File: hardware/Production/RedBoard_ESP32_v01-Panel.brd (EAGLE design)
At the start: 246.1 x 248.9 mm, 2478 parts, among them J1 5.5x2.1mm Barrel, J101 USB C, J102 USB_SOLDER_PADS, J103 M10NO_SILK, J108 QWIIC_RIGHT_ANGLE, J109 MICRO-SD-PUSH-PUSH-EXT-PIN, J110 5.5x2.1mm Barrel, J117 USB C, J118 USB_SOLDER_PADS, J119 M10NO_SILK, J124 QWIIC_RIGHT_ANGLE, J125 MICRO-SD-PUSH-PUSH-EXT-PIN, J126 5.5x2.1mm Barrel, J13 QWIIC_RIGHT_ANGLE, J133 USB C, J134 USB_SOLDER_PADS, J135 M10NO_SILK, J140 QWIIC_RIGHT_ANGLE, J141 MICRO-SD-PUSH-PUSH-EXT-PIN, J142 5.5x2.1mm Barrel, J149 USB C, J15 MICRO-SD-PUSH-PUSH-EXT-PIN, J150 USB_SOLDER_PADS, J151 M10NO_SILK, J156 QWIIC_RIGHT_ANGLE, J157 MICRO-SD-PUSH-PUSH-EXT-PIN, J158 5.5x2.1mm Barrel, J165 USB C, J166 USB_SOLDER_PADS, J167 M10NO_SILK, J172 QWIIC_RIGHT_ANGLE, J173 MICRO-SD-PUSH-PUSH-EXT-PIN, J174 5.5x2.1mm Barrel, J181 USB C, J182 USB_SOLDER_PADS, J183 M10NO_SILK, J188 QWIIC_RIGHT_ANGLE, J189 MICRO-SD-PUSH-PUSH-EXT-PIN, J190 5.5x2.1mm Barrel, J2 USB C, J21 USB C, J22 USB_SOLDER_PADS, J23 M10NO_SILK, J28 QWIIC_RIGHT_ANGLE, J29 MICRO-SD-PUSH-PUSH-EXT-PIN, J3 USB_SOLDER_PADS, J30 5.5x2.1mm Barrel, J37 USB C, J38 USB_SOLDER_PADS, J39 M10NO_SILK, J44 QWIIC_RIGHT_ANGLE, J45 MICRO-SD-PUSH-PUSH-EXT-PIN, J46 5.5x2.1mm Barrel, J5 M10NO_SILK, J53 USB C, J54 USB_SOLDER_PADS, J55 M10NO_SILK, J60 QWIIC_RIGHT_ANGLE, J61 MICRO-SD-PUSH-PUSH-EXT-PIN, J62 5.5x2.1mm Barrel, J69 USB C, J70 USB_SOLDER_PADS, J71 M10NO_SILK, J76 QWIIC_RIGHT_ANGLE, J77 MICRO-SD-PUSH-PUSH-EXT-PIN, J78 5.5x2.1mm Barrel, J85 USB C, J86 USB_SOLDER_PADS, J87 M10NO_SILK, J92 QWIIC_RIGHT_ANGLE, J93 MICRO-SD-PUSH-PUSH-EXT-PIN, J94 5.5x2.1mm Barrel, Q1 MBT3904DW1T1, Q100 20V/4.2A/52mΩ/1.4W, Q102 20V/4.2A/52mΩ/1.4W, Q104 20V/4.2A/52mΩ/1.4W, Q105 MBT3904DW1T1, Q107 20V/4.2A/52mΩ/1.4W, Q109 20V/4.2A/52mΩ/1.4W, Q11 20V/4.2A/52mΩ/1.4W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

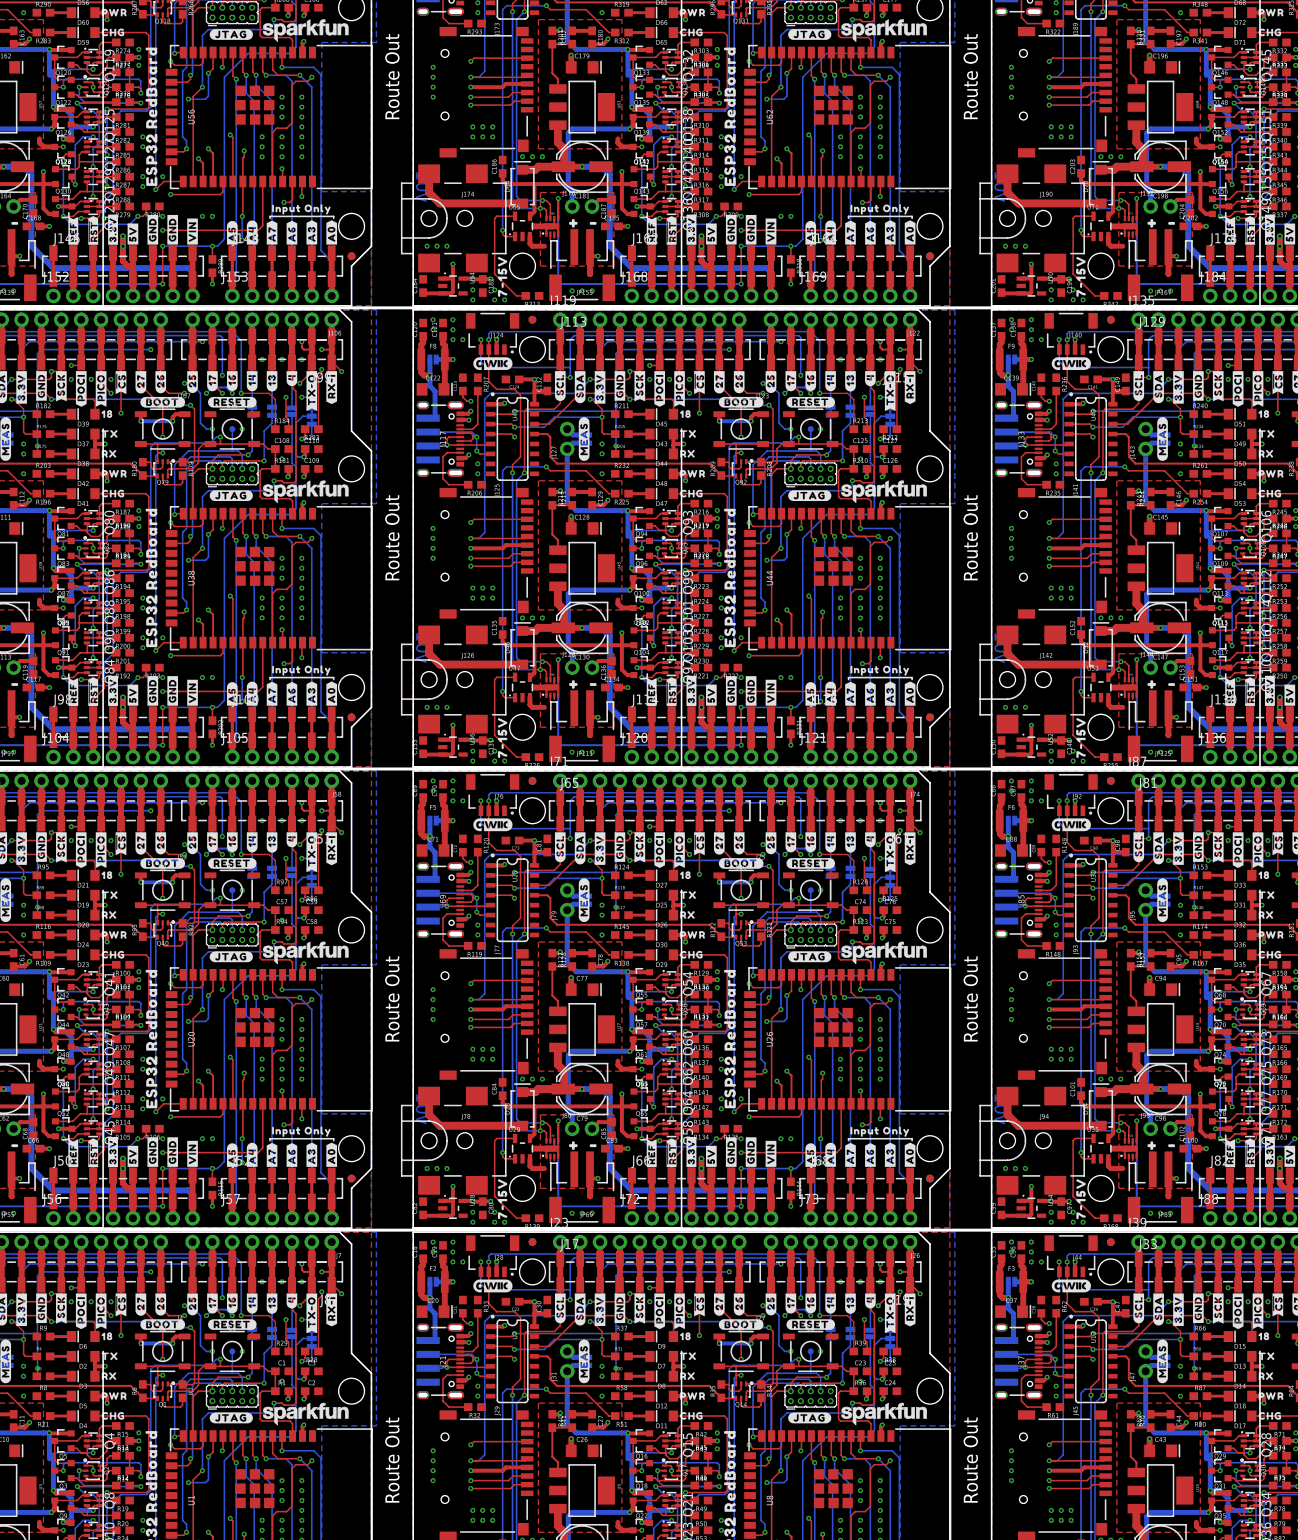
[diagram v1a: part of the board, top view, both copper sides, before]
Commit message: Fixed trace on bottom side, regenerated panel file.
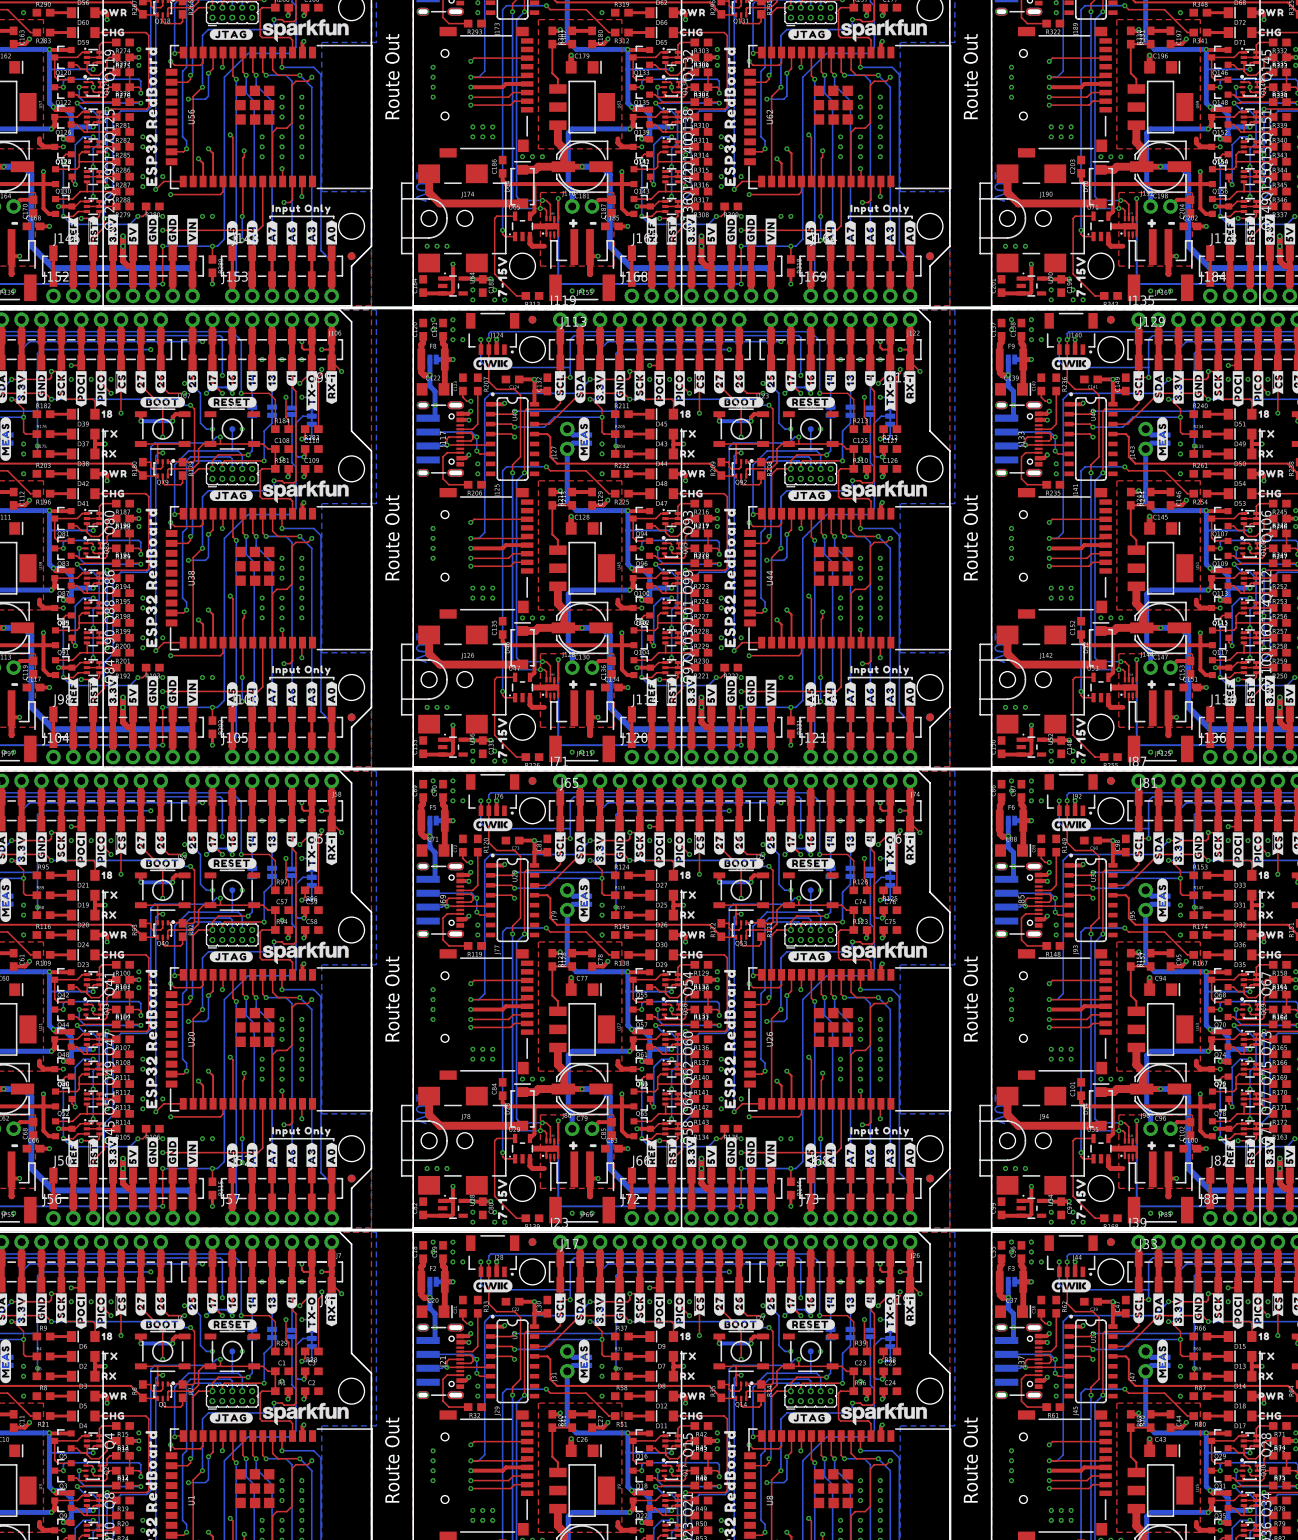
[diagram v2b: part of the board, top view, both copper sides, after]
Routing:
- net 5V_MEAS1: track 65.2 -> 64.6 mm
- net 5V_MEAS8: track 65.2 -> 64.6 mm
- net 5V_MEAS5: track 65.2 -> 64.6 mm
- net 5V_MEAS4: track 65.2 -> 64.6 mm
- net 5V_MEAS10: track 65.2 -> 64.6 mm
- net 5V_MEAS: track 65.2 -> 64.6 mm
- net 5V_MEAS9: track 65.2 -> 64.6 mm
- net 5V_MEAS7: track 65.2 -> 64.6 mm
- net 5V_MEAS6: track 65.2 -> 64.6 mm
- net 5V_MEAS3: track 65.2 -> 64.6 mm
- net 5V_MEAS11: track 65.2 -> 64.6 mm
- net 5V_MEAS2: track 65.2 -> 64.6 mm

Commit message: Changed labels as suggested by Chris; updated production files.
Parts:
- added U$1141: (no value), output-ESP32:#13#TCK#32321869
- added U$1142: (no value), output-ESP32:#14#TMS#32321869
- added U$1143: (no value), output-ESP32:#16#32321869
- added U$1144: (no value), output-ESP32:#17#32321869
- added U$1145: (no value), output-ESP32:#25#32321869
- added U$1146: (no value), output-ESP32:#26#32321869
- added U$1147: (no value), output-ESP32:#5##CS##32321869
- added U$1148: (no value), output-ESP32:#23#PICO#321866
- added U$1149: (no value), output-ESP32:#19#POCI#321866
- added U$1150: (no value), output-ESP32:#18#SCK#32321869
- added U$1151: (no value), output-ESP32:#21#SDA#32321869
- added U$1152: (no value), output-ESP32:#22#SCL#32321869
- added U$1153: (no value), output-ESP32:#27#32321869
- added U$1154: (no value), output-ESP32:#GND#321866
- added U$1155: (no value), output-ESP32:#3#3V#321866
- added U$1156: (no value), output-ESP32:#MEAS#1851
- added U$1157: (no value), output-ESP32:#BYP#35
- added U$1158: (no value), output-ESP32:D#32321863
- added U$1159: (no value), output-ESP32:D#32321862
- added U$1160: (no value), output-ESP32:G32321864
- added U$1161: (no value), output-ESP32:#1849
- added U$1162: (no value), output-ESP32:#1850
- added U$1163: (no value), output-ESP32:#I2C#1855
- added U$1164: (no value), output-ESP32:##ALERT##1852
- added U$1165: (no value), output-ESP32:#TMS#1854
- added U$1166: (no value), output-ESP32:#TCK#1853
- added U$1167, U$1168: (no value), output-ESP32:INPUT_ONLY321867
- added U$1169: (no value), output-ESP32:##ALERT##4#321866
- added U$1170: (no value), output-ESP32:TP1321868
- added U$1171: (no value), SparkFun-Aesthetics:REDBOARD_LOGO
- added U$1172: (no value), output-ESP32:#IOT#132321869
- added U$1173: (no value), output-ESP32:ESP32321856
- added U$1174: (no value), output-ESP32:#IOT#132321874
- added U$1175: (no value), output-ESP32:MADE_IN32321857
- added U$1176: (no value), output-ESP32:THE_USA32321858
- U$100, U$290: device output-ESP32:#GND#32 -> output-ESP32:#IOT#132321869
- U$1000: device output-ESP32:#34#A6#32321865 -> output-ESP32:#14#14
- U$1001: device output-ESP32:#35#A7#321862 -> output-ESP32:#13#5
- U$1002: device output-ESP32:#32#A4#32321865 -> output-ESP32:#4#2
- U$1003: device output-ESP32:#34#A6#321862 -> output-ESP32:#TX#O#0
- U$1004: device output-ESP32:#VIN#321862 -> output-ESP32:#RX#I#1
- U$1005, U$1103: device output-ESP32:#GND#321863 -> output-ESP32:#RESET#1842
- U$1006: device output-ESP32:#5V#321864 -> output-ESP32:#BOOT#1841
- U$1007, U$437: device output-ESP32:#3#3V#321864 -> output-ESP32:#JTAG#1847
- U$1008, U$910: device output-ESP32:#GND#321863 -> output-ESP32:#A0#1843
- U$1009: device output-ESP32:##RESET##321864 -> output-ESP32:#A3#1843
- U$101: device output-ESP32:#SCK#31 -> output-ESP32:#SDA#33
- U$1010: device output-ESP32:#IOREF#321865 -> output-ESP32:#A6#1843
- U$1011: device output-ESP32:#3#RX#I#32321869 -> output-ESP32:#A7#1843
- U$1012: device output-ESP32:#1#TX#O#32321869 -> output-ESP32:#A4#1843
- U$1013: device output-ESP32:#13#TCK#32321869 -> output-ESP32:#A5#1843
- U$1014: device output-ESP32:#14#TMS#32321869 -> output-ESP32:#VIN#1843
- U$1015: device output-ESP32:#16#32321869 -> output-ESP32:#GND#1844
- U$1016: device output-ESP32:#17#32321869 -> output-ESP32:#GND#1844
- U$1017: device output-ESP32:#25#32321869 -> output-ESP32:#5V#1845
- U$1018: device output-ESP32:#26#32321869 -> output-ESP32:#3#3V#1845
- U$1019: device output-ESP32:#5##CS##32321869 -> output-ESP32:##RST##1845
- U$102: device output-ESP32:#POCI#30 -> output-ESP32:#3#3V#33
- U$1020: device output-ESP32:#23#PICO#321866 -> output-ESP32:#REF#1846
- U$1021: device output-ESP32:#19#POCI#321866 -> output-ESP32:#MEAS#1851
- U$1022: device output-ESP32:#18#SCK#32321869 -> output-ESP32:#1849
- U$1023: device output-ESP32:#21#SDA#32321869 -> output-ESP32:#1850
- U$1024: device output-ESP32:#22#SCL#32321869 -> output-ESP32:#BATT#1848
- U$1025: device output-ESP32:#27#32321869 -> output-ESP32:#JTAG#1847
- U$1026: device output-ESP32:#GND#321866 -> output-ESP32:ESP321855
- U$1027: device output-ESP32:#3#3V#321866 -> output-ESP32:7#15V32321861
- U$1028: device output-ESP32:#MEAS#1851 -> output-ESP32:#39#A3#321862
- U$1029: device output-ESP32:#BYP#35 -> output-ESP32:#36#A0#321862
- U$103: device output-ESP32:#PICO#29 -> output-ESP32:#GND#32
- U$1030: device output-ESP32:D#32321863 -> output-ESP32:#34#A6#32321865
- U$1031: device output-ESP32:D#32321862 -> output-ESP32:#35#A7#321862
- U$1032: device output-ESP32:G32321864 -> output-ESP32:#32#A4#32321865
- U$1033: device output-ESP32:#1849 -> output-ESP32:#34#A6#321862
- U$1034: device output-ESP32:#1850 -> output-ESP32:#VIN#321862
- U$1035, U$940: device output-ESP32:#I2C#1855 -> output-ESP32:#GND#321863
- U$1036: device output-ESP32:##ALERT##1852 -> output-ESP32:#5V#321864
- U$1037: device output-ESP32:#TMS#1854 -> output-ESP32:#3#3V#321864
- U$1038, U$1133: device output-ESP32:#TCK#1853 -> output-ESP32:#GND#321863
- U$1039: device output-ESP32:MADE_IN_THE_USA321857 -> output-ESP32:##RESET##321864
- U$104: device output-ESP32:1836 -> output-ESP32:#SCK#31
- U$1040: device output-ESP32:ESP32_REDBOARD321857 -> output-ESP32:#IOREF#321865
- U$1041: device output-ESP32:REDBOARD321856 -> output-ESP32:#3#RX#I#32321869
- U$1042: device output-ESP32:INPUT_ONLY321867 -> output-ESP32:#1#TX#O#32321869
- U$1043: device output-ESP32:INPUT_ONLY321867 -> output-ESP32:#13#TCK#32321869
- U$1044: device output-ESP32:##ALERT##4#321866 -> output-ESP32:#14#TMS#32321869
- U$1045: device output-ESP32:TP1321868 -> output-ESP32:#16#32321869
- U$1046: device output-ESP32:V323252 -> output-ESP32:#17#32321869
- U$1047: device output-ESP32:#SCL#34 -> output-ESP32:#25#32321869
- U$1048: device output-ESP32:#SDA#33 -> output-ESP32:#26#32321869
- U$1049: device output-ESP32:#3#3V#33 -> output-ESP32:#5##CS##32321869
- U$105: device output-ESP32:##CS##28 -> output-ESP32:#POCI#30
- U$1050: device output-ESP32:#GND#32 -> output-ESP32:#23#PICO#321866
- U$1051: device output-ESP32:#SCK#31 -> output-ESP32:#19#POCI#321866
- U$1052: device output-ESP32:#POCI#30 -> output-ESP32:#18#SCK#32321869
- U$1053: device output-ESP32:#PICO#29 -> output-ESP32:#21#SDA#32321869
- U$1054: device output-ESP32:1836 -> output-ESP32:#22#SCL#32321869
- U$1055: device output-ESP32:##CS##28 -> output-ESP32:#27#32321869
- U$1056: device output-ESP32:#27#27 -> output-ESP32:#GND#321866
- U$1057: device output-ESP32:#26#26 -> output-ESP32:#3#3V#321866
- U$1058: device output-ESP32:TX1838 -> output-ESP32:#MEAS#1851
- U$1059: device output-ESP32:RX1839 -> output-ESP32:#BYP#35
- U$106: device output-ESP32:#27#27 -> output-ESP32:#PICO#29
- U$1060: device output-ESP32:PWR1837 -> output-ESP32:D#32321863
- U$1061: device output-ESP32:CHG1840 -> output-ESP32:D#32321862
- U$1062: device output-ESP32:#25#18 -> output-ESP32:G32321864
- U$1063: device output-ESP32:#17#17 -> output-ESP32:#1849
- U$1064: device output-ESP32:#16#15 -> output-ESP32:#1850
- U$1065: device output-ESP32:#14#14 -> output-ESP32:#I2C#1855
- U$1066: device output-ESP32:#13#5 -> output-ESP32:##ALERT##1852
- U$1067: device output-ESP32:#4#2 -> output-ESP32:#TMS#1854
- U$1068: device output-ESP32:#TX#O#0 -> output-ESP32:#TCK#1853
- U$1069: device output-ESP32:#RX#I#1 -> output-ESP32:INPUT_ONLY321867
- U$107: device output-ESP32:#26#26 -> output-ESP32:1836
- U$1070: device output-ESP32:#RESET#1842 -> output-ESP32:INPUT_ONLY321867
- U$1071: device output-ESP32:#BOOT#1841 -> output-ESP32:##ALERT##4#321866
- U$1072: device output-ESP32:#JTAG#1847 -> output-ESP32:TP1321868
- U$1073: device output-ESP32:#A0#1843 -> SparkFun-Aesthetics:REDBOARD_LOGO
- U$1074: device output-ESP32:#A3#1843 -> output-ESP32:#IOT#132321869
- U$1075: device output-ESP32:#A6#1843 -> output-ESP32:ESP32321856
- U$1076: device output-ESP32:#A7#1843 -> output-ESP32:#IOT#132321874
- U$1077: device output-ESP32:#A4#1843 -> output-ESP32:MADE_IN32321857
- U$1078: device output-ESP32:#A5#1843 -> output-ESP32:THE_USA32321858
- U$1079: device output-ESP32:#VIN#1843 -> output-ESP32:V323252
- U$108: device output-ESP32:TX1838 -> output-ESP32:##CS##28
- U$1080: device output-ESP32:#GND#1844 -> output-ESP32:#SCL#34
- U$1081: device output-ESP32:#GND#1844 -> output-ESP32:#SDA#33
- U$1082: device output-ESP32:#5V#1845 -> output-ESP32:#3#3V#33
- U$1083: device output-ESP32:#3#3V#1845 -> output-ESP32:#GND#32
- U$1084: device output-ESP32:##RST##1845 -> output-ESP32:#SCK#31
- U$1085: device output-ESP32:#REF#1846 -> output-ESP32:#POCI#30
- U$1086: device output-ESP32:#MEAS#1851 -> output-ESP32:#PICO#29
- U$1087: device output-ESP32:#1849 -> output-ESP32:1836
- U$1088: device output-ESP32:#1850 -> output-ESP32:##CS##28
- U$1089: device output-ESP32:#BATT#1848 -> output-ESP32:#27#27
- U$109: device output-ESP32:RX1839 -> output-ESP32:#27#27
- U$1090, U$502: device output-ESP32:#JTAG#1847 -> output-ESP32:#26#26
- U$1091: device output-ESP32:ESP321855 -> output-ESP32:TX1838
- U$1092: device output-ESP32:7#15V32321861 -> output-ESP32:RX1839
- U$1093: device output-ESP32:#39#A3#321862 -> output-ESP32:PWR1837
- U$1094: device output-ESP32:#36#A0#321862 -> output-ESP32:CHG1840
- U$1095: device output-ESP32:#34#A6#32321865 -> output-ESP32:#25#18
- U$1096: device output-ESP32:#35#A7#321862 -> output-ESP32:#17#17
- U$1097: device output-ESP32:#32#A4#32321865 -> output-ESP32:#16#15
- U$1098: device output-ESP32:#34#A6#321862 -> output-ESP32:#14#14
- U$1099: device output-ESP32:#VIN#321862 -> output-ESP32:#13#5
- U$110: device output-ESP32:PWR1837 -> output-ESP32:#26#26
- U$1100: device output-ESP32:#GND#321863 -> output-ESP32:#4#2
- U$1101: device output-ESP32:#5V#321864 -> output-ESP32:#TX#O#0
- U$1102: device output-ESP32:#3#3V#321864 -> output-ESP32:#RX#I#1
- U$1104: device output-ESP32:##RESET##321864 -> output-ESP32:#BOOT#1841
- U$1105, U$535: device output-ESP32:#IOREF#321865 -> output-ESP32:#JTAG#1847
- U$1106: device output-ESP32:#3#RX#I#32321869 -> output-ESP32:#A0#1843
- U$1107: device output-ESP32:#1#TX#O#32321869 -> output-ESP32:#A3#1843
- U$1108: device output-ESP32:#13#TCK#32321869 -> output-ESP32:#A6#1843
- U$1109: device output-ESP32:#14#TMS#32321869 -> output-ESP32:#A7#1843
- U$111: device output-ESP32:CHG1840 -> output-ESP32:TX1838
- U$1110: device output-ESP32:#16#32321869 -> output-ESP32:#A4#1843
- U$1111: device output-ESP32:#17#32321869 -> output-ESP32:#A5#1843
- U$1112: device output-ESP32:#25#32321869 -> output-ESP32:#VIN#1843
- U$1113: device output-ESP32:#26#32321869 -> output-ESP32:#GND#1844
- U$1114: device output-ESP32:#5##CS##32321869 -> output-ESP32:#GND#1844
- U$1115: device output-ESP32:#23#PICO#321866 -> output-ESP32:#5V#1845
- U$1116: device output-ESP32:#19#POCI#321866 -> output-ESP32:#3#3V#1845
- U$1117: device output-ESP32:#18#SCK#32321869 -> output-ESP32:##RST##1845
- U$1118: device output-ESP32:#21#SDA#32321869 -> output-ESP32:#REF#1846
- U$1119: device output-ESP32:#22#SCL#32321869 -> output-ESP32:#MEAS#1851
- U$112: device output-ESP32:#25#18 -> output-ESP32:RX1839
- U$1120: device output-ESP32:#27#32321869 -> output-ESP32:#1849
- U$1121: device output-ESP32:#GND#321866 -> output-ESP32:#1850
- U$1122: device output-ESP32:#3#3V#321866 -> output-ESP32:#BATT#1848
- U$1123: device output-ESP32:#MEAS#1851 -> output-ESP32:#JTAG#1847
- U$1124: device output-ESP32:#BYP#35 -> output-ESP32:ESP321855
- U$1125: device output-ESP32:D#32321863 -> output-ESP32:7#15V32321861
- U$1126: device output-ESP32:D#32321862 -> output-ESP32:#39#A3#321862
- U$1127: device output-ESP32:G32321864 -> output-ESP32:#36#A0#321862
- U$1128: device output-ESP32:#1849 -> output-ESP32:#34#A6#32321865
- U$1129: device output-ESP32:#1850 -> output-ESP32:#35#A7#321862
- U$113: device output-ESP32:#17#17 -> output-ESP32:PWR1837
- U$1130: device output-ESP32:#I2C#1855 -> output-ESP32:#32#A4#32321865
- U$1131: device output-ESP32:##ALERT##1852 -> output-ESP32:#34#A6#321862
- U$1132: device output-ESP32:#TMS#1854 -> output-ESP32:#VIN#321862
- U$1134: device output-ESP32:MADE_IN_THE_USA321857 -> output-ESP32:#5V#321864
- U$1135: device output-ESP32:ESP32_REDBOARD321857 -> output-ESP32:#3#3V#321864
- U$1136: device output-ESP32:REDBOARD321856 -> output-ESP32:#GND#321863
- U$1137: device output-ESP32:INPUT_ONLY321867 -> output-ESP32:##RESET##321864
- U$1138: device output-ESP32:INPUT_ONLY321867 -> output-ESP32:#IOREF#321865
- U$1139: device output-ESP32:##ALERT##4#321866 -> output-ESP32:#3#RX#I#32321869
- U$114: device output-ESP32:#16#15 -> output-ESP32:CHG1840
- U$1140: device output-ESP32:TP1321868 -> output-ESP32:#1#TX#O#32321869
- U$115: device output-ESP32:#14#14 -> output-ESP32:#25#18
- U$116: device output-ESP32:#13#5 -> output-ESP32:#17#17
- U$117: device output-ESP32:#4#2 -> output-ESP32:#16#15
- U$118: device output-ESP32:#TX#O#0 -> output-ESP32:#14#14
- U$119: device output-ESP32:#RX#I#1 -> output-ESP32:#13#5
- U$120: device output-ESP32:#RESET#1842 -> output-ESP32:#4#2
- U$121: device output-ESP32:#BOOT#1841 -> output-ESP32:#TX#O#0
- U$122, U$710: device output-ESP32:#JTAG#1847 -> output-ESP32:#RX#I#1
- U$123: device output-ESP32:#A0#1843 -> output-ESP32:#RESET#1842
- U$124: device output-ESP32:#A3#1843 -> output-ESP32:#BOOT#1841
- U$125: device output-ESP32:#A6#1843 -> output-ESP32:#JTAG#1847
- U$126: device output-ESP32:#A7#1843 -> output-ESP32:#A0#1843
- U$127: device output-ESP32:#A4#1843 -> output-ESP32:#A3#1843
- U$128: device output-ESP32:#A5#1843 -> output-ESP32:#A6#1843
- U$129: device output-ESP32:#VIN#1843 -> output-ESP32:#A7#1843
- U$130: device output-ESP32:#GND#1844 -> output-ESP32:#A4#1843
- U$131: device output-ESP32:#GND#1844 -> output-ESP32:#A5#1843
- U$132: device output-ESP32:#5V#1845 -> output-ESP32:#VIN#1843
- U$133: device output-ESP32:#3#3V#1845 -> output-ESP32:#GND#1844
- U$134: device output-ESP32:##RST##1845 -> output-ESP32:#GND#1844
- U$135: device output-ESP32:#REF#1846 -> output-ESP32:#5V#1845
- U$136: device output-ESP32:#MEAS#1851 -> output-ESP32:#3#3V#1845
- U$137: device output-ESP32:#1849 -> output-ESP32:##RST##1845
- U$138: device output-ESP32:#1850 -> output-ESP32:#REF#1846
- U$139: device output-ESP32:#BATT#1848 -> output-ESP32:#MEAS#1851
- U$140: device output-ESP32:#JTAG#1847 -> output-ESP32:#1849
- U$141: device output-ESP32:ESP321855 -> output-ESP32:#1850
- U$142: device output-ESP32:7#15V32321861 -> output-ESP32:#BATT#1848
- U$143, U$713: device output-ESP32:#39#A3#321862 -> output-ESP32:#JTAG#1847
- U$144: device output-ESP32:#36#A0#321862 -> output-ESP32:ESP321855
- U$145: device output-ESP32:#34#A6#32321865 -> output-ESP32:7#15V32321861
- U$146: device output-ESP32:#35#A7#321862 -> output-ESP32:#39#A3#321862
- U$147: device output-ESP32:#32#A4#32321865 -> output-ESP32:#36#A0#321862
- U$148: device output-ESP32:#34#A6#321862 -> output-ESP32:#34#A6#32321865
- U$149: device output-ESP32:#VIN#321862 -> output-ESP32:#35#A7#321862
- U$150, U$248: device output-ESP32:#GND#321863 -> output-ESP32:#32#A4#32321865
- U$151: device output-ESP32:#5V#321864 -> output-ESP32:#34#A6#321862
- U$152: device output-ESP32:#3#3V#321864 -> output-ESP32:#VIN#321862
- U$154: device output-ESP32:##RESET##321864 -> output-ESP32:#5V#321864
- U$155: device output-ESP32:#IOREF#321865 -> output-ESP32:#3#3V#321864
- U$156, U$251: device output-ESP32:#3#RX#I#32321869 -> output-ESP32:#GND#321863
- U$157: device output-ESP32:#1#TX#O#32321869 -> output-ESP32:##RESET##321864
- U$158: device output-ESP32:#13#TCK#32321869 -> output-ESP32:#IOREF#321865
- U$159: device output-ESP32:#14#TMS#32321869 -> output-ESP32:#3#RX#I#32321869
- U$160: device output-ESP32:#16#32321869 -> output-ESP32:#1#TX#O#32321869
- U$161: device output-ESP32:#17#32321869 -> output-ESP32:#13#TCK#32321869
- U$162: device output-ESP32:#25#32321869 -> output-ESP32:#14#TMS#32321869
- U$163: device output-ESP32:#26#32321869 -> output-ESP32:#16#32321869
- U$164: device output-ESP32:#5##CS##32321869 -> output-ESP32:#17#32321869
- U$165: device output-ESP32:#23#PICO#321866 -> output-ESP32:#25#32321869
- U$166: device output-ESP32:#19#POCI#321866 -> output-ESP32:#26#32321869
- U$167: device output-ESP32:#18#SCK#32321869 -> output-ESP32:#5##CS##32321869
- U$168: device output-ESP32:#21#SDA#32321869 -> output-ESP32:#23#PICO#321866
- U$169: device output-ESP32:#22#SCL#32321869 -> output-ESP32:#19#POCI#321866
- U$170: device output-ESP32:#27#32321869 -> output-ESP32:#18#SCK#32321869
- U$171: device output-ESP32:#GND#321866 -> output-ESP32:#21#SDA#32321869
- U$172: device output-ESP32:#3#3V#321866 -> output-ESP32:#22#SCL#32321869
- U$173: device output-ESP32:#MEAS#1851 -> output-ESP32:#27#32321869
- U$174: device output-ESP32:#BYP#35 -> output-ESP32:#GND#321866
- U$175: device output-ESP32:D#32321863 -> output-ESP32:#3#3V#321866
- U$176: device output-ESP32:D#32321862 -> output-ESP32:#MEAS#1851
- U$177: device output-ESP32:G32321864 -> output-ESP32:#BYP#35
- U$178: device output-ESP32:#1849 -> output-ESP32:D#32321863
- U$179: device output-ESP32:#1850 -> output-ESP32:D#32321862
- U$180: device output-ESP32:#I2C#1855 -> output-ESP32:G32321864
- U$181: device output-ESP32:##ALERT##1852 -> output-ESP32:#1849
- U$182: device output-ESP32:#TMS#1854 -> output-ESP32:#1850
- U$183: device output-ESP32:#TCK#1853 -> output-ESP32:#I2C#1855
- U$184: device output-ESP32:MADE_IN_THE_USA321857 -> output-ESP32:##ALERT##1852
- U$185: device output-ESP32:ESP32_REDBOARD321857 -> output-ESP32:#TMS#1854
- U$186: device output-ESP32:REDBOARD321856 -> output-ESP32:#TCK#1853
- U$191: device output-ESP32:V323252 -> SparkFun-Aesthetics:REDBOARD_LOGO
- U$192: device output-ESP32:#SCL#34 -> output-ESP32:#IOT#132321869
- U$193: device output-ESP32:#SDA#33 -> output-ESP32:ESP32321856
- U$194: device output-ESP32:#3#3V#33 -> output-ESP32:#IOT#132321874
- U$195: device output-ESP32:#GND#32 -> output-ESP32:MADE_IN32321857
- U$196: device output-ESP32:#SCK#31 -> output-ESP32:THE_USA32321858
- U$197: device output-ESP32:#POCI#30 -> output-ESP32:V323252
- U$198: device output-ESP32:#PICO#29 -> output-ESP32:#SCL#34
- U$199: device output-ESP32:1836 -> output-ESP32:#SDA#33
- U$200: device output-ESP32:##CS##28 -> output-ESP32:#3#3V#33
- U$201: device output-ESP32:#27#27 -> output-ESP32:#GND#32
- U$202: device output-ESP32:#26#26 -> output-ESP32:#SCK#31
- U$203: device output-ESP32:TX1838 -> output-ESP32:#POCI#30
- U$204: device output-ESP32:RX1839 -> output-ESP32:#PICO#29
- U$205: device output-ESP32:PWR1837 -> output-ESP32:1836
- U$206: device output-ESP32:CHG1840 -> output-ESP32:##CS##28
- U$207: device output-ESP32:#25#18 -> output-ESP32:#27#27
- U$208: device output-ESP32:#17#17 -> output-ESP32:#26#26
- U$209: device output-ESP32:#16#15 -> output-ESP32:TX1838
- U$210: device output-ESP32:#14#14 -> output-ESP32:RX1839
- U$211: device output-ESP32:#13#5 -> output-ESP32:PWR1837
- U$212: device output-ESP32:#4#2 -> output-ESP32:CHG1840
- U$213: device output-ESP32:#TX#O#0 -> output-ESP32:#25#18
- U$214: device output-ESP32:#RX#I#1 -> output-ESP32:#17#17
- U$215: device output-ESP32:#RESET#1842 -> output-ESP32:#16#15
- U$216: device output-ESP32:#BOOT#1841 -> output-ESP32:#14#14
- U$217, U$805: device output-ESP32:#JTAG#1847 -> output-ESP32:#13#5
- U$218: device output-ESP32:#A0#1843 -> output-ESP32:#4#2
- U$219: device output-ESP32:#A3#1843 -> output-ESP32:#TX#O#0
- U$220: device output-ESP32:#A6#1843 -> output-ESP32:#RX#I#1
- U$221: device output-ESP32:#A7#1843 -> output-ESP32:#RESET#1842
- U$222: device output-ESP32:#A4#1843 -> output-ESP32:#BOOT#1841
- U$223: device output-ESP32:#A5#1843 -> output-ESP32:#JTAG#1847
- U$224: device output-ESP32:#VIN#1843 -> output-ESP32:#A0#1843
- U$225: device output-ESP32:#GND#1844 -> output-ESP32:#A3#1843
- U$226: device output-ESP32:#GND#1844 -> output-ESP32:#A6#1843
- U$227: device output-ESP32:#5V#1845 -> output-ESP32:#A7#1843
- U$228: device output-ESP32:#3#3V#1845 -> output-ESP32:#A4#1843
- U$229: device output-ESP32:##RST##1845 -> output-ESP32:#A5#1843
- U$230: device output-ESP32:#REF#1846 -> output-ESP32:#VIN#1843
- U$231: device output-ESP32:#MEAS#1851 -> output-ESP32:#GND#1844
- U$232: device output-ESP32:#1849 -> output-ESP32:#GND#1844
- U$233: device output-ESP32:#1850 -> output-ESP32:#5V#1845
- U$234: device output-ESP32:#BATT#1848 -> output-ESP32:#3#3V#1845
- U$235: device output-ESP32:#JTAG#1847 -> output-ESP32:##RST##1845
- U$236: device output-ESP32:ESP321855 -> output-ESP32:#REF#1846
- U$237: device output-ESP32:7#15V32321861 -> output-ESP32:#MEAS#1851
- U$238: device output-ESP32:#39#A3#321862 -> output-ESP32:#1849
- U$239: device output-ESP32:#36#A0#321862 -> output-ESP32:#1850
- U$240: device output-ESP32:#34#A6#32321865 -> output-ESP32:#BATT#1848
- U$241, U$811: device output-ESP32:#35#A7#321862 -> output-ESP32:#JTAG#1847
- U$242: device output-ESP32:#32#A4#32321865 -> output-ESP32:ESP321855
- U$243: device output-ESP32:#34#A6#321862 -> output-ESP32:7#15V32321861
- U$244: device output-ESP32:#VIN#321862 -> output-ESP32:#39#A3#321862
- U$245, U$343: device output-ESP32:#GND#321863 -> output-ESP32:#36#A0#321862
- U$246: device output-ESP32:#5V#321864 -> output-ESP32:#34#A6#32321865
- U$247: device output-ESP32:#3#3V#321864 -> output-ESP32:#35#A7#321862
- U$249: device output-ESP32:##RESET##321864 -> output-ESP32:#34#A6#321862
- U$250: device output-ESP32:#IOREF#321865 -> output-ESP32:#VIN#321862
- U$252: device output-ESP32:#1#TX#O#32321869 -> output-ESP32:#5V#321864
- U$253: device output-ESP32:#13#TCK#32321869 -> output-ESP32:#3#3V#321864
- U$254, U$349: device output-ESP32:#14#TMS#32321869 -> output-ESP32:#GND#321863
- U$255: device output-ESP32:#16#32321869 -> output-ESP32:##RESET##321864
- U$256: device output-ESP32:#17#32321869 -> output-ESP32:#IOREF#321865
- U$257: device output-ESP32:#25#32321869 -> output-ESP32:#3#RX#I#32321869
- U$258: device output-ESP32:#26#32321869 -> output-ESP32:#1#TX#O#32321869
- U$259: device output-ESP32:#5##CS##32321869 -> output-ESP32:#13#TCK#32321869
- U$260: device output-ESP32:#23#PICO#321866 -> output-ESP32:#14#TMS#32321869
- U$261: device output-ESP32:#19#POCI#321866 -> output-ESP32:#16#32321869
- U$262: device output-ESP32:#18#SCK#32321869 -> output-ESP32:#17#32321869
- U$263: device output-ESP32:#21#SDA#32321869 -> output-ESP32:#25#32321869
- U$264: device output-ESP32:#22#SCL#32321869 -> output-ESP32:#26#32321869
- U$265: device output-ESP32:#27#32321869 -> output-ESP32:#5##CS##32321869
- U$266: device output-ESP32:#GND#321866 -> output-ESP32:#23#PICO#321866
- U$267: device output-ESP32:#3#3V#321866 -> output-ESP32:#19#POCI#321866
- U$268: device output-ESP32:#MEAS#1851 -> output-ESP32:#18#SCK#32321869
- U$269: device output-ESP32:#BYP#35 -> output-ESP32:#21#SDA#32321869
- U$270: device output-ESP32:D#32321863 -> output-ESP32:#22#SCL#32321869
- U$271: device output-ESP32:D#32321862 -> output-ESP32:#27#32321869
- U$272: device output-ESP32:G32321864 -> output-ESP32:#GND#321866
- U$273: device output-ESP32:#1849 -> output-ESP32:#3#3V#321866
- U$274: device output-ESP32:#1850 -> output-ESP32:#MEAS#1851
- U$275: device output-ESP32:#I2C#1855 -> output-ESP32:#BYP#35
- U$276: device output-ESP32:##ALERT##1852 -> output-ESP32:D#32321863
- U$277: device output-ESP32:#TMS#1854 -> output-ESP32:D#32321862
- U$278: device output-ESP32:#TCK#1853 -> output-ESP32:G32321864
- U$279: device output-ESP32:MADE_IN_THE_USA321857 -> output-ESP32:#1849
- U$280: device output-ESP32:ESP32_REDBOARD321857 -> output-ESP32:#1850
- U$281: device output-ESP32:REDBOARD321856 -> output-ESP32:#I2C#1855
- U$282: device output-ESP32:INPUT_ONLY321867 -> output-ESP32:##ALERT##1852
- U$283: device output-ESP32:INPUT_ONLY321867 -> output-ESP32:#TMS#1854
- U$284: device output-ESP32:##ALERT##4#321866 -> output-ESP32:#TCK#1853
- U$285: device output-ESP32:TP1321868 -> output-ESP32:INPUT_ONLY321867
- U$286: device output-ESP32:V323252 -> output-ESP32:INPUT_ONLY321867
- U$287: device output-ESP32:#SCL#34 -> output-ESP32:##ALERT##4#321866
- U$288: device output-ESP32:#SDA#33 -> output-ESP32:TP1321868
- U$289: device output-ESP32:#3#3V#33 -> SparkFun-Aesthetics:REDBOARD_LOGO
- U$291: device output-ESP32:#SCK#31 -> output-ESP32:ESP32321856
- U$292: device output-ESP32:#POCI#30 -> output-ESP32:#IOT#132321874
- U$293: device output-ESP32:#PICO#29 -> output-ESP32:MADE_IN32321857
- U$294: device output-ESP32:1836 -> output-ESP32:THE_USA32321858
- U$295: device output-ESP32:##CS##28 -> output-ESP32:V323252
- U$296: device output-ESP32:#27#27 -> output-ESP32:#SCL#34
- U$297: device output-ESP32:#26#26 -> output-ESP32:#SDA#33
- U$298: device output-ESP32:TX1838 -> output-ESP32:#3#3V#33
- U$299: device output-ESP32:RX1839 -> output-ESP32:#GND#32
- U$300: device output-ESP32:PWR1837 -> output-ESP32:#SCK#31
- U$301: device output-ESP32:CHG1840 -> output-ESP32:#POCI#30
- U$302: device output-ESP32:#25#18 -> output-ESP32:#PICO#29
- U$303: device output-ESP32:#17#17 -> output-ESP32:1836
- U$304: device output-ESP32:#16#15 -> output-ESP32:##CS##28
- U$305: device output-ESP32:#14#14 -> output-ESP32:#27#27
- U$306: device output-ESP32:#13#5 -> output-ESP32:#26#26
- U$307: device output-ESP32:#4#2 -> output-ESP32:TX1838
- U$308: device output-ESP32:#TX#O#0 -> output-ESP32:RX1839
- U$309: device output-ESP32:#RX#I#1 -> output-ESP32:PWR1837
- U$310: device output-ESP32:#RESET#1842 -> output-ESP32:CHG1840
- U$311: device output-ESP32:#BOOT#1841 -> output-ESP32:#25#18
- U$312, U$900: device output-ESP32:#JTAG#1847 -> output-ESP32:#17#17
- U$313: device output-ESP32:#A0#1843 -> output-ESP32:#16#15
- U$314: device output-ESP32:#A3#1843 -> output-ESP32:#14#14
- U$315: device output-ESP32:#A6#1843 -> output-ESP32:#13#5
- U$316: device output-ESP32:#A7#1843 -> output-ESP32:#4#2
- U$317: device output-ESP32:#A4#1843 -> output-ESP32:#TX#O#0
- U$318: device output-ESP32:#A5#1843 -> output-ESP32:#RX#I#1
- U$319: device output-ESP32:#VIN#1843 -> output-ESP32:#RESET#1842
- U$320: device output-ESP32:#GND#1844 -> output-ESP32:#BOOT#1841
- U$321: device output-ESP32:#GND#1844 -> output-ESP32:#JTAG#1847
- U$322: device output-ESP32:#5V#1845 -> output-ESP32:#A0#1843
- U$323: device output-ESP32:#3#3V#1845 -> output-ESP32:#A3#1843
- U$324: device output-ESP32:##RST##1845 -> output-ESP32:#A6#1843
- U$325: device output-ESP32:#REF#1846 -> output-ESP32:#A7#1843
- U$326: device output-ESP32:#MEAS#1851 -> output-ESP32:#A4#1843
- U$327: device output-ESP32:#1849 -> output-ESP32:#A5#1843
- U$328: device output-ESP32:#1850 -> output-ESP32:#VIN#1843
- U$329: device output-ESP32:#BATT#1848 -> output-ESP32:#GND#1844
- U$330: device output-ESP32:#JTAG#1847 -> output-ESP32:#GND#1844
- U$331: device output-ESP32:ESP321855 -> output-ESP32:#5V#1845
- U$332: device output-ESP32:7#15V32321861 -> output-ESP32:#3#3V#1845
- U$333: device output-ESP32:#39#A3#321862 -> output-ESP32:##RST##1845
- U$334: device output-ESP32:#36#A0#321862 -> output-ESP32:#REF#1846
- U$335: device output-ESP32:#34#A6#32321865 -> output-ESP32:#MEAS#1851
- U$336: device output-ESP32:#35#A7#321862 -> output-ESP32:#1849
- U$337: device output-ESP32:#32#A4#32321865 -> output-ESP32:#1850
- U$338: device output-ESP32:#34#A6#321862 -> output-ESP32:#BATT#1848
- U$339, U$909: device output-ESP32:#VIN#321862 -> output-ESP32:#JTAG#1847
- U$340, U$438: device output-ESP32:#GND#321863 -> output-ESP32:ESP321855
- U$341: device output-ESP32:#5V#321864 -> output-ESP32:7#15V32321861
- U$342: device output-ESP32:#3#3V#321864 -> output-ESP32:#39#A3#321862
- U$344: device output-ESP32:##RESET##321864 -> output-ESP32:#34#A6#32321865
- U$345: device output-ESP32:#IOREF#321865 -> output-ESP32:#35#A7#321862
- U$346: device output-ESP32:#3#RX#I#32321869 -> output-ESP32:#32#A4#32321865
- U$347: device output-ESP32:#1#TX#O#32321869 -> output-ESP32:#34#A6#321862
- U$348: device output-ESP32:#13#TCK#32321869 -> output-ESP32:#VIN#321862
- U$350: device output-ESP32:#16#32321869 -> output-ESP32:#5V#321864
- U$351: device output-ESP32:#17#32321869 -> output-ESP32:#3#3V#321864
- U$352, U$447: device output-ESP32:#25#32321869 -> output-ESP32:#GND#321863
- U$353: device output-ESP32:#26#32321869 -> output-ESP32:##RESET##321864
- U$354: device output-ESP32:#5##CS##32321869 -> output-ESP32:#IOREF#321865
- U$355: device output-ESP32:#23#PICO#321866 -> output-ESP32:#3#RX#I#32321869
- U$356: device output-ESP32:#19#POCI#321866 -> output-ESP32:#1#TX#O#32321869
- U$357: device output-ESP32:#18#SCK#32321869 -> output-ESP32:#13#TCK#32321869
- U$358: device output-ESP32:#21#SDA#32321869 -> output-ESP32:#14#TMS#32321869
- U$359: device output-ESP32:#22#SCL#32321869 -> output-ESP32:#16#32321869
- U$360: device output-ESP32:#27#32321869 -> output-ESP32:#17#32321869
- U$361: device output-ESP32:#GND#321866 -> output-ESP32:#25#32321869
- U$362: device output-ESP32:#3#3V#321866 -> output-ESP32:#26#32321869
- U$363: device output-ESP32:#MEAS#1851 -> output-ESP32:#5##CS##32321869
- U$364: device output-ESP32:#BYP#35 -> output-ESP32:#23#PICO#321866
- U$365: device output-ESP32:D#32321863 -> output-ESP32:#19#POCI#321866
- U$366: device output-ESP32:D#32321862 -> output-ESP32:#18#SCK#32321869
- U$367: device output-ESP32:G32321864 -> output-ESP32:#21#SDA#32321869
- U$368: device output-ESP32:#1849 -> output-ESP32:#22#SCL#32321869
- U$369: device output-ESP32:#1850 -> output-ESP32:#27#32321869
- U$370: device output-ESP32:#I2C#1855 -> output-ESP32:#GND#321866
- U$371: device output-ESP32:##ALERT##1852 -> output-ESP32:#3#3V#321866
- U$372: device output-ESP32:#TMS#1854 -> output-ESP32:#MEAS#1851
- U$373: device output-ESP32:#TCK#1853 -> output-ESP32:#BYP#35
- U$374: device output-ESP32:MADE_IN_THE_USA321857 -> output-ESP32:D#32321863
- U$375: device output-ESP32:ESP32_REDBOARD321857 -> output-ESP32:D#32321862
- U$376: device output-ESP32:REDBOARD321856 -> output-ESP32:G32321864
- U$377: device output-ESP32:INPUT_ONLY321867 -> output-ESP32:#1849
- U$378: device output-ESP32:INPUT_ONLY321867 -> output-ESP32:#1850
- U$379: device output-ESP32:##ALERT##4#321866 -> output-ESP32:#I2C#1855
- U$380: device output-ESP32:TP1321868 -> output-ESP32:##ALERT##1852
- U$381: device output-ESP32:V323252 -> output-ESP32:#TMS#1854
- U$382: device output-ESP32:#SCL#34 -> output-ESP32:#TCK#1853
- U$383: device output-ESP32:#SDA#33 -> output-ESP32:INPUT_ONLY321867
- U$384: device output-ESP32:#3#3V#33 -> output-ESP32:INPUT_ONLY321867
- U$385: device output-ESP32:#GND#32 -> output-ESP32:##ALERT##4#321866
- U$386: device output-ESP32:#SCK#31 -> output-ESP32:TP1321868
- U$387: device output-ESP32:#POCI#30 -> SparkFun-Aesthetics:REDBOARD_LOGO
- U$388: device output-ESP32:#PICO#29 -> output-ESP32:#IOT#132321869
- U$389: device output-ESP32:1836 -> output-ESP32:ESP32321856
- U$390: device output-ESP32:##CS##28 -> output-ESP32:#IOT#132321874
- U$391: device output-ESP32:#27#27 -> output-ESP32:MADE_IN32321857
- U$392: device output-ESP32:#26#26 -> output-ESP32:THE_USA32321858
- U$393: device output-ESP32:TX1838 -> output-ESP32:V323252
- U$394: device output-ESP32:RX1839 -> output-ESP32:#SCL#34
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
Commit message: Updated silkscreen.
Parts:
- moved LOGO1 24.6 mm to (48.9, 13.3)
- moved LOGO11 24.6 mm to (196.7, 13.3)
- moved LOGO5 24.6 mm to (122.8, 13.3)
- moved LOGO16 24.6 mm to (48.9, 72.3)
- moved LOGO21 24.6 mm to (122.8, 72.3)
- moved LOGO26 24.6 mm to (196.7, 72.3)
- moved LOGO31 24.6 mm to (48.9, 131.2)
- moved LOGO36 24.6 mm to (122.8, 131.2)
- moved LOGO41 24.6 mm to (196.7, 131.2)
- moved LOGO46 24.6 mm to (48.9, 190.1)
- moved LOGO51 24.6 mm to (122.8, 190.1)
- moved LOGO56 24.6 mm to (196.7, 190.1)
- moved U$684 11.3 mm to (26.2, 150.5)
- moved U$782 11.3 mm to (100.1, 150.5)
- moved U$880 11.3 mm to (174.0, 150.5)
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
